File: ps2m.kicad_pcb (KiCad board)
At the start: 2 copper layers, 6 parts, among them P1 MOUSE_PORT, P2 MINI_DIN_6, U1 PIC16(L)F627-xxI/SS

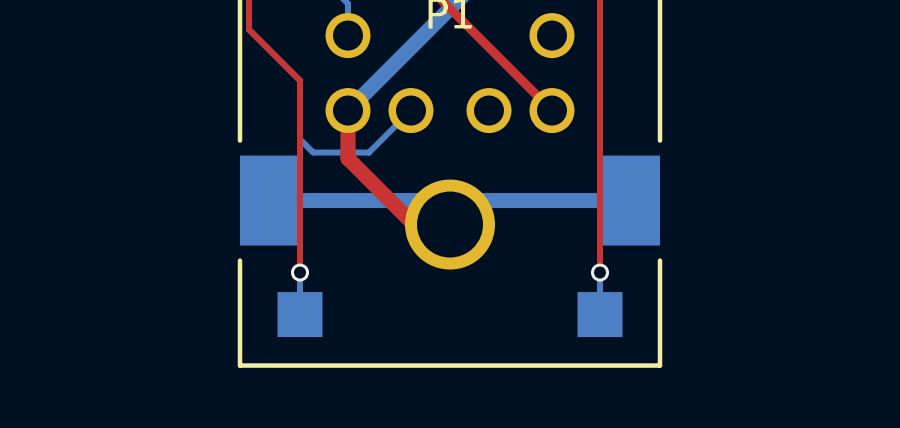
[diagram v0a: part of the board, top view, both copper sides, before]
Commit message: Rounded edges of PCB, TOP side note
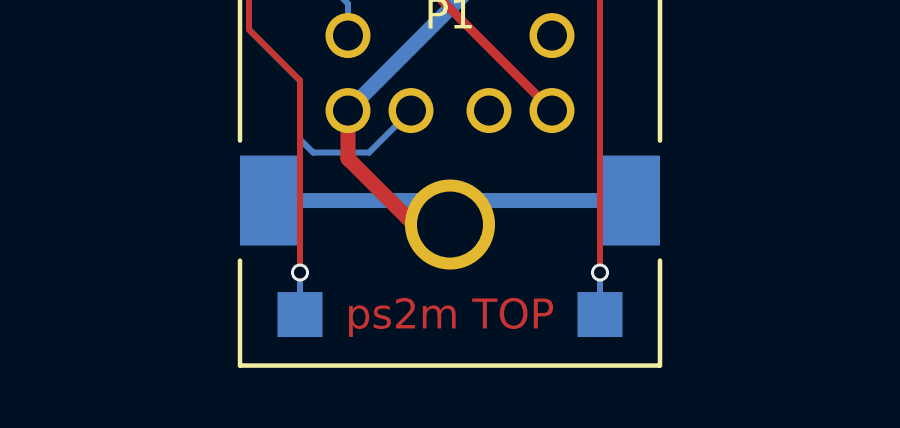
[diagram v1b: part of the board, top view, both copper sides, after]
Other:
- board text added: "ps2m TOP"
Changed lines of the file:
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@@
 (kicad_pcb (version 4) (host pcbnew 4.0.5)
   (general
-    (links 23)
+    (links 0)
     (no_connects 0)
-    (area 0 0 0 0)
+    (area 134.724999 78.224999 167.275001 115.775)
     (thickness 1.6)
-    (drawings 32)
+    (drawings 37)
     (tracks 151)
     (zones 0)
@@
   (page A4)
   (layers
-    (0 F.Cu signal)
+    (0 F.Cu signal hide)
     (31 B.Cu signal hide)
     (32 B.Adhes user)
@@
     (47 F.CrtYd user)
     (48 B.Fab user hide)
-    (49 F.Fab user hide)
+    (49 F.Fab user)
   )
   (setup
-    (last_trace_width 0.5)
+    (last_trace_width 0.2)
     (user_trace_width 0.2)
     (user_trace_width 0.3)
@@
     (pad_to_mask_clearance 0.2)
     (aux_axis_origin 0 0)
-    (visible_elements 7FFCFFFF)
+    (visible_elements 7FFCFF7F)
     (pcbplotparams
       (layerselection 0x02cc0_80000001)
@@
       (net 9 /MOUSE_9))
   )
+  (gr_arc (start 157.25 86.25) (end 157.25 85.5) (angle 90) (layer Margin) (width 0.2))
+  (gr_arc (start 144.75 86.25) (end 144 86.25) (angle 90) (layer Margin) (width 0.2))
+  (gr_arc (start 144.75 112.75) (end 144.75 113.5) (angle 90) (layer Margin) (width 0.2))
+  (gr_arc (start 157.25 112.75) (end 158 112.75) (angle 90) (layer Margin) (width 0.2))
+  (gr_text "ps2m TOP" (at 151 112) (layer F.Cu)
+    (effects (font (size 1 1) (thickness 0.15)))
+  )
   (gr_text P1 (at 150.5 90) (layer Eco1.User)
     (effects (font (size 1.5 1.5) (thickness 0.3)))
@@
   (gr_line (start 148.2 92.7) (end 149.1 93.6) (layer Eco2.User) (width 0.2))
   (gr_line (start 148.2 86.3) (end 148.2 92.7) (layer Eco2.User) (width 0.2))
-  (gr_line (start 144 113.5) (end 158 113.5) (layer Margin) (width 0.2))
-  (gr_line (start 144 85.5) (end 158 85.5) (layer Margin) (width 0.2))
-  (gr_line (start 144 113.5) (end 144 85.5) (layer Margin) (width 0.2))
-  (gr_line (start 158 113.5) (end 158 85.5) (layer Margin) (width 0.2))
+  (gr_line (start 144.75 113.5) (end 157.25 113.5) (layer Margin) (width 0.2))
+  (gr_line (start 144.75 85.5) (end 157.25 85.5) (layer Margin) (width 0.2))
+  (gr_line (start 144 112.75) (end 144 86.25) (layer Margin) (width 0.2))
+  (gr_line (start 158 112.75) (end 158 86.25) (layer Margin) (width 0.2))
   (segment (start 151.4 91.8) (end 152.7 90.5) (width 0.3) (layer B.Cu) (net 1))
   (segment (start 150.656421 92.543579) (end 151.4 91.8) (width 0.3) (layer F.Cu) (net 1))
